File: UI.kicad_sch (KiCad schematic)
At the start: 8 parts, among them SW501 SW_Push, SW502 SW_Push

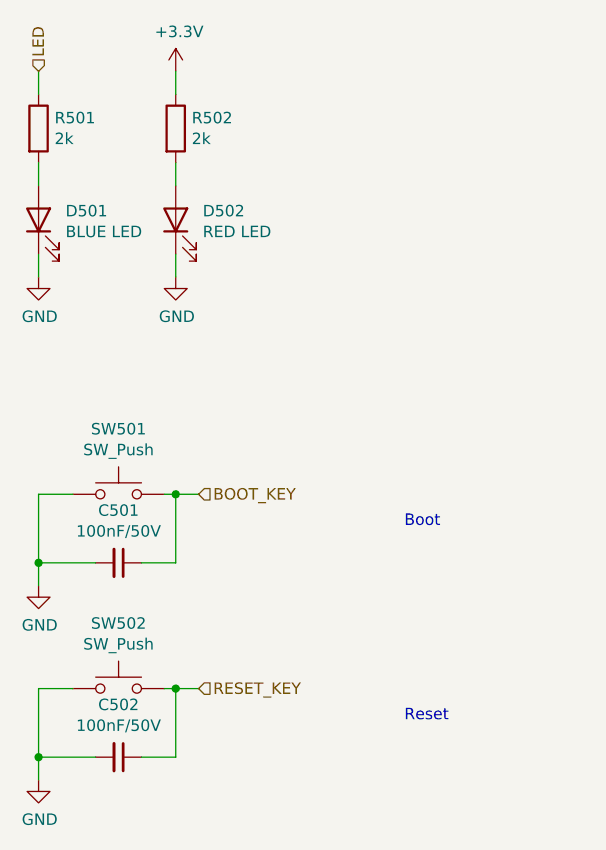
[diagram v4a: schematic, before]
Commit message: Go back to ISO1050 for CAN transceiver
Also add CAN RX and TX LEDs and beef up buck capacitors
as much as space allows.
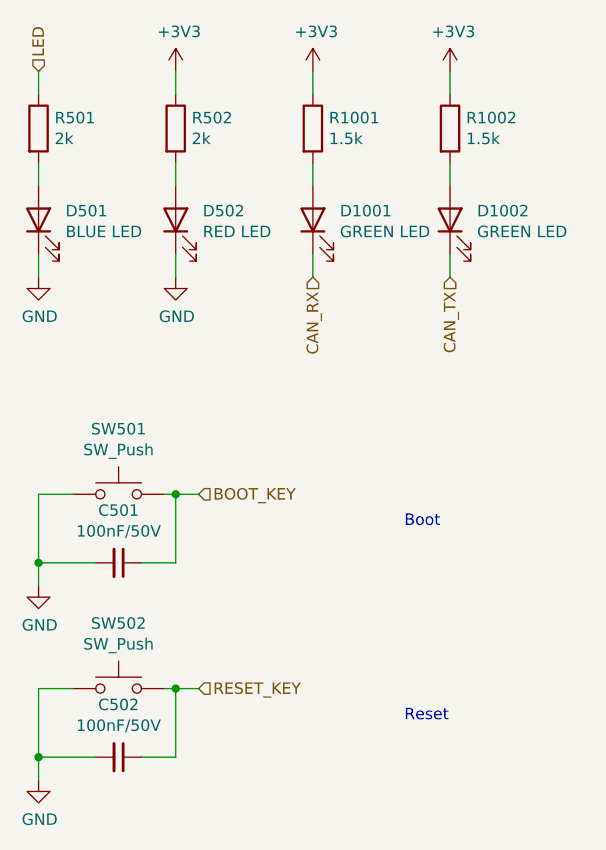
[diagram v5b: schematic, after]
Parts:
- added D1001, D1002: GREEN LED, LED_SMD:LED_0603_1608Metric, symbol Device:LED
- added R1001, R1002: 1.5k, Resistor_SMD:R_0402_1005Metric, symbol Device:R
- D501: LCSC C72041 -> C7496819
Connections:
- net +3V3: now also R1001.1, R1002.1
- new net: D1001.2 (A), R1001.2
- new net: D1002.2 (A), R1002.2
- new net CAN_RX: D1001.1 (K)
- new net CAN_TX: D1002.1 (K)
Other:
- company: Hat Labs Ltd -> Hat Labs Oy
- title: Sailor Hat with ESP32 -> SH-ESP32
